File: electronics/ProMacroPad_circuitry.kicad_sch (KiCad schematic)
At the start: 8 parts, among them J1 Conn_01x06, J2 Conn_01x07, P1 Conn_02x20_Odd_Even, U1 quad_level_shifter

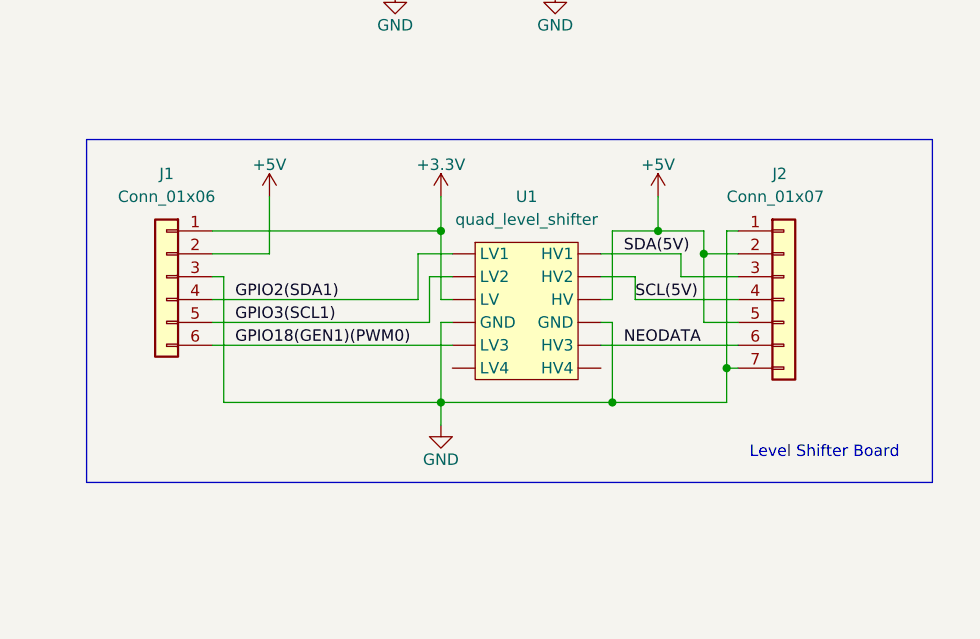
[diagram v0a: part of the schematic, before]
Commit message: Split apart connectors for LCD and keypad neopixel strip in the schematic
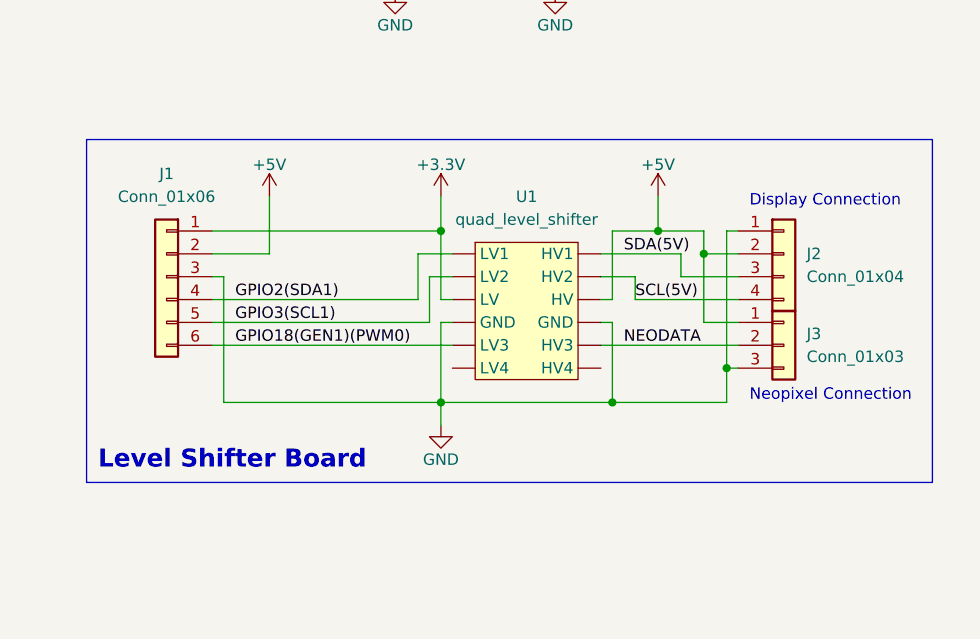
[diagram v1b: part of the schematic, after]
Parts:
- removed J2: Conn_01x07, Connector_PinHeader_2.54mm:PinHeader_1x05_P2.54mm_Vertical, symbol Connector_Generic:Conn_01x07
- added J2: Conn_01x04, Connector_PinHeader_2.54mm:PinHeader_1x04_P2.54mm_Vertical, symbol Connector_Generic:Conn_01x04
- added J3: Conn_01x03, Connector_PinHeader_2.54mm:PinHeader_1x03_P2.54mm_Vertical, symbol Connector_Generic:Conn_01x03
- P1: now left out of the parts list
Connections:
- net +5V: now also J2.2 (Pin_2), J3.1 (Pin_1)
- net GND: now also J2.1 (Pin_1), J3.3 (Pin_3)
- net NEODATA: now also J3.2 (Pin_2)
- net SCL(5V): now also J2.4 (Pin_4)
- net SDA(5V): now also J2.3 (Pin_3)
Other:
- note added: "Display Connection"
- note added: "Neopixel Connection"
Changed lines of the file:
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@@
     (effects (font (size 1.27 1.27)) (justify left bottom))
   )
-  (text "Level Shifter Board" (at 97.79 132.08 0)
+  (text "Display Connection\n" (at 97.79 104.14 0)
+    (effects (font (size 1.27 1.27)) (justify left bottom))
+  )
+  (text "Level Shifter Board" (at 25.4 133.35 0)
+    (effects (font (size 2 2) (thickness 0.254) bold) (justify left bottom))
+  )
+  (text "Neopixel Connection" (at 97.79 125.73 0)
     (effects (font (size 1.27 1.27)) (justify left bottom))
   )
@@
   (symbol (lib_id "power:+5V") (at 78.74 24.13 0) (unit 1)
     (in_bom yes) (on_board yes)
-    (property "Reference" "#PWR01" (id 0) (at 78.74 27.94 0)
+    (property "Reference" "#PWR07" (id 0) (at 78.74 27.94 0)
       (effects (font (size 1.27 1.27)) hide)
     )
@@
   (symbol (lib_id "power:+3.3V") (at 55.88 24.13 0) (unit 1)
     (in_bom yes) (on_board yes)
-    (property "Reference" "#PWR04" (id 0) (at 55.88 27.94 0)
+    (property "Reference" "#PWR02" (id 0) (at 55.88 27.94 0)
       (effects (font (size 1.27 1.27)) hide)
     )
@@
   (symbol (lib_id "power:GND") (at 76.2 80.01 0) (unit 1)
     (in_bom yes) (on_board yes)
-    (property "Reference" "#PWR02" (id 0) (at 76.2 86.36 0)
+    (property "Reference" "#PWR06" (id 0) (at 76.2 86.36 0)
       (effects (font (size 1.27 1.27)) hide)
     )
@@
   )
   (symbol (lib_id "Connector_Generic:Conn_02x20_Odd_Even") (at 66.04 50.8 0) (unit 1)
-    (in_bom yes) (on_board yes)
+    (in_bom no) (on_board no)
     (property "Reference" "P1" (id 0) (at 67.31 22.4282 0))
     (property "Value" "Conn_02x20_Odd_Even" (id 1) (at 67.31 24.7396 0))
@@
   (symbol (lib_id "power:+3.3V") (at 63.5 102.87 0) (unit 1)
     (in_bom yes) (on_board yes)
-    (property "Reference" "#PWR06" (id 0) (at 63.5 106.68 0)
+    (property "Reference" "#PWR04" (id 0) (at 63.5 106.68 0)
       (effects (font (size 1.27 1.27)) hide)
     )
@@
     (property "Datasheet" "" (id 3) (at 63.5 102.87 0))
     (pin "1")
+  )
+  (symbol (lib_id "Connector_Generic:Conn_01x03") (at 101.6 119.38 0) (unit 1)
+    (in_bom yes) (on_board yes) (fields_autoplaced)
+    (property "Reference" "J3" (id 0) (at 104.14 118.1099 0)
+      (effects (font (size 1.27 1.27)) (justify left))
+    )
+    (property "Value" "Conn_01x03" (id 1) (at 104.14 120.6499 0)
+      (effects (font (size 1.27 1.27)) (justify left))
+    )
+    (property "Footprint" "Connector_PinHeader_2.54mm:PinHeader_1x03_P2.54mm_Vertical" (id 2) (at 101.6 119.38 0)
+      (effects (font (size 1.27 1.27)) hide)
+    )
+    (property "Datasheet" "~" (id 3) (at 101.6 119.38 0)
+      (effects (font (size 1.27 1.27)) hide)
+    )
+    (pin "1")
+    (pin "2")
+    (pin "3")
   )
   (symbol (lib_id "Connector_Generic:Conn_01x06") (at 33.02 111.76 0) (mirror y) (unit 1)
@@
     (pin "6")
   )
-  (symbol (lib_id "Connector_Generic:Conn_01x07") (at 101.6 114.3 0) (unit 1)
-    (in_bom yes) (on_board yes)
-    (property "Reference" "J2" (id 0) (at 100.33 100.33 0)
-      (effects (font (size 1.27 1.27)) (justify left))
-    )
-    (property "Value" "Conn_01x07" (id 1) (at 95.25 102.87 0)
-      (effects (font (size 1.27 1.27)) (justify left))
-    )
-    (property "Footprint" "Connector_PinHeader_2.54mm:PinHeader_1x05_P2.54mm_Vertical" (id 2) (at 101.6 114.3 0)
-      (effects (font (size 1.27 1.27)) hide)
-    )
-    (property "Datasheet" "~" (id 3) (at 101.6 114.3 0)
-      (effects (font (size 1.27 1.27)) hide)
-    )
-    (pin "1")
-    (pin "2")
-    (pin "3")
-    (pin "4")
-    (pin "5")
-    (pin "6")
-    (pin "7")
-  )
   (symbol (lib_id "power:+5V") (at 44.45 102.87 0) (unit 1)
     (in_bom yes) (on_board yes)
-    (property "Reference" "#PWR05" (id 0) (at 44.45 106.68 0)
+    (property "Reference" "#PWR01" (id 0) (at 44.45 106.68 0)
       (effects (font (size 1.27 1.27)) hide)
     )
@@
   (symbol (lib_id "power:GND") (at 63.5 128.27 0) (unit 1)
     (in_bom yes) (on_board yes)
-    (property "Reference" "#PWR07" (id 0) (at 63.5 134.62 0)
+    (property "Reference" "#PWR05" (id 0) (at 63.5 134.62 0)
       (effects (font (size 1.27 1.27)) hide)
     )
@@
     (pin "")
   )
+  (symbol (lib_id "Connector_Generic:Conn_01x04") (at 101.6 109.22 0) (unit 1)
+    (in_bom yes) (on_board yes) (fields_autoplaced)
+    (property "Reference" "J2" (id 0) (at 104.14 109.2199 0)
+      (effects (font (size 1.27 1.27)) (justify left))
+    )
+    (property "Value" "Conn_01x04" (id 1) (at 104.14 111.7599 0)
+      (effects (font (size 1.27 1.27)) (justify left))
+    )
+    (property "Footprint" "Connector_PinHeader_2.54mm:PinHeader_1x04_P2.54mm_Vertical" (id 2) (at 101.6 109.22 0)
+      (effects (font (size 1.27 1.27)) hide)
+    )
+    (property "Datasheet" "~" (id 3) (at 101.6 109.22 0)
+      (effects (font (size 1.27 1.27)) hide)
+    )
+    (pin "1")
+    (pin "2")
+    (pin "3")
+    (pin "4")
+  )
   (sheet_instances
     (path "/" (page "1"))
   )
   (symbol_instances
-    (path "/00000000-0000-0000-0000-0000580c1b61"
+    (path "/9eacbb2d-50b8-4118-adfc-424ecd01793d"
       (reference "#PWR01") (unit 1) (value "+5V") (footprint "")
     )
-    (path "/00000000-0000-0000-0000-0000580c1d11"
-      (reference "#PWR02") (unit 1) (value "GND") (footprint "")
+    (path "/00000000-0000-0000-0000-0000580c1bc1"
+      (reference "#PWR02") (unit 1) (value "+3.3V") (footprint "")
     )
     (path "/00000000-0000-0000-0000-0000580c1e01"
       (reference "#PWR03") (unit 1) (value "GND") (footprint "")
     )
-    (path "/00000000-0000-0000-0000-0000580c1bc1"
+    (path "/2e9e347b-3a58-4bc6-a17d-c08a993af17a"
       (reference "#PWR04") (unit 1) (value "+3.3V") (footprint "")
     )
-    (path "/9eacbb2d-50b8-4118-adfc-424ecd01793d"
-      (reference "#PWR05") (unit 1) (value "+5V") (footprint "")
-    )
-    (path "/2e9e347b-3a58-4bc6-a17d-c08a993af17a"
-      (reference "#PWR06") (unit 1) (value "+3.3V") (footprint "")
-    )
     (path "/e8685b3e-eccd-4437-baaf-b2ee6240a83c"
-      (reference "#PWR07") (unit 1) (value "GND") (footprint "")
+      (reference "#PWR05") (unit 1) (value "GND") (footprint "")
+    )
+    (path "/00000000-0000-0000-0000-0000580c1d11"
+      (reference "#PWR06") (unit 1) (value "GND") (footprint "")
+    )
+    (path "/00000000-0000-0000-0000-0000580c1b61"
+      (reference "#PWR07") (unit 1) (value "+5V") (footprint "")
     )
     (path "/c6c3c7e1-1d0c-40e9-a9b5-621b98f4c1e6"
@@
       (reference "J1") (unit 1) (value "Conn_01x06") (footprint "Connector_PinHeader_2.54mm:PinHeader_1x06_P2.54mm_Vertical")
     )
-    (path "/986b7e4d-ecdc-467f-b1ac-492727860f1f"
-      (reference "J2") (unit 1) (value "Conn_01x07") (footprint "Connector_PinHeader_2.54mm:PinHeader_1x05_P2.54mm_Vertical")
+    (path "/f91c8543-b6dd-4522-a7f9-22fa2740e79b"
+      (reference "J2") (unit 1) (value "Conn_01x04") (footprint "Connector_PinHeader_2.54mm:PinHeader_1x04_P2.54mm_Vertical")
+    )
+    (path "/68d756a1-f19e-4dc7-a5af-e5afa6b979ac"
+      (reference "J3") (unit 1) (value "Conn_01x03") (footprint "Connector_PinHeader_2.54mm:PinHeader_1x03_P2.54mm_Vertical")
     )
     (path "/00000000-0000-0000-0000-00005834fb2e"

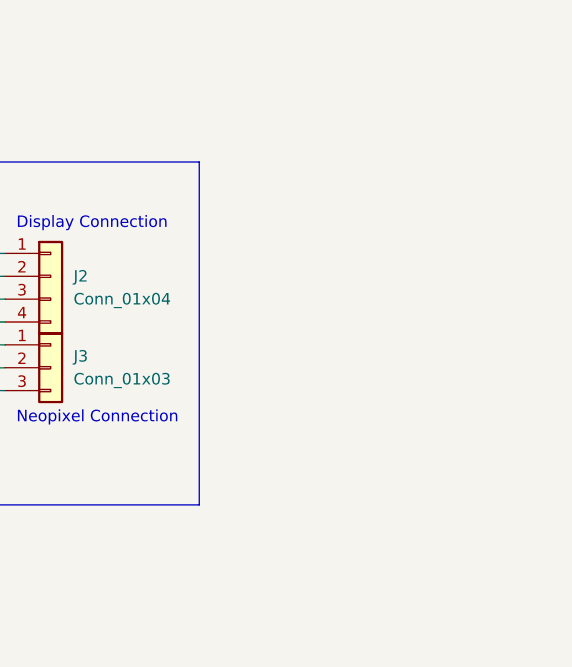
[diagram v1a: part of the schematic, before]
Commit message: added keypad matrix connectors to schematic
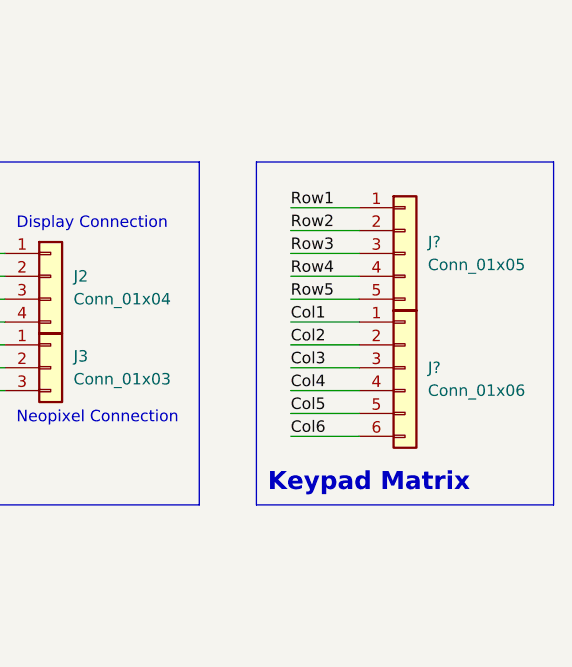
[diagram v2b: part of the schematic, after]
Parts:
- added J?: Conn_01x06, symbol Connector_Generic:Conn_01x06
- added J?: Conn_01x05, symbol Connector_Generic:Conn_01x05
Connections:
- new net Col1: J?.1 (Pin_1)
- new net Col2: J?.2 (Pin_2)
- new net Col3: J?.3 (Pin_3)
- new net Col4: J?.4 (Pin_4)
- new net Col5: J?.5 (Pin_5)
- new net Col6: J?.6 (Pin_6)
- new net Row1: J?.1 (Pin_1)
- new net Row2: J?.2 (Pin_2)
- new net Row3: J?.3 (Pin_3)
- new net Row4: J?.4 (Pin_4)
- new net Row5: J?.5 (Pin_5)
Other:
- note added: "Keypad Matrix"
- title: (none) -> ProMacroPad
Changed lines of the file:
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@@
   (paper "A4")
   (title_block
-    (date "15 nov 2012")
+    (title "ProMacroPad")
+    (date "2022-01-20")
   )
   (junction (at 82.55 125.73) (diameter 0) (color 0 0 0 0)
@@
   (junction (at 63.5 125.73) (diameter 0) (color 0 0 0 0)
   )
+  (wire (pts (xy 128.27 114.3) (xy 135.89 114.3))
+    (stroke (width 0) (type default) (color 0 0 0 0))
+  )
   (wire (pts (xy 92.71 109.22) (xy 92.71 116.84))
     (stroke (width 0) (type default) (color 0 0 0 0))
@@
     (stroke (width 0) (type default) (color 0 0 0 0))
   )
+  (wire (pts (xy 128.27 101.6) (xy 135.89 101.6))
+    (stroke (width 0) (type default) (color 0 0 0 0))
+  )
+  (wire (pts (xy 128.27 111.76) (xy 135.89 111.76))
+    (stroke (width 0) (type default) (color 0 0 0 0))
+  )
+  (polyline (pts (xy 124.46 96.52) (xy 157.48 96.52))
+    (stroke (width 0) (type default) (color 0 0 0 0))
+  )
   (wire (pts (xy 81.28 116.84) (xy 82.55 116.84))
     (stroke (width 0) (type default) (color 0 0 0 0))
@@
     (stroke (width 0) (type solid) (color 0 0 0 0))
   )
+  (wire (pts (xy 128.27 124.46) (xy 135.89 124.46))
+    (stroke (width 0) (type default) (color 0 0 0 0))
+  )
   (wire (pts (xy 60.96 60.96) (xy 31.75 60.96))
     (stroke (width 0) (type solid) (color 0 0 0 0))
@@
     (stroke (width 0) (type solid) (color 0 0 0 0))
   )
+  (wire (pts (xy 128.27 106.68) (xy 135.89 106.68))
+    (stroke (width 0) (type default) (color 0 0 0 0))
+  )
   (wire (pts (xy 60.96 30.48) (xy 31.75 30.48))
     (stroke (width 0) (type solid) (color 0 0 0 0))
@@
     (stroke (width 0) (type solid) (color 0 0 0 0))
   )
+  (wire (pts (xy 128.27 109.22) (xy 135.89 109.22))
+    (stroke (width 0) (type default) (color 0 0 0 0))
+  )
   (wire (pts (xy 95.25 121.92) (xy 95.25 125.73))
     (stroke (width 0) (type default) (color 0 0 0 0))
@@
     (stroke (width 0) (type default) (color 0 0 0 0))
   )
+  (wire (pts (xy 128.27 119.38) (xy 135.89 119.38))
+    (stroke (width 0) (type default) (color 0 0 0 0))
+  )
   (wire (pts (xy 38.1 109.22) (xy 44.45 109.22))
     (stroke (width 0) (type default) (color 0 0 0 0))
   )
+  (wire (pts (xy 128.27 104.14) (xy 135.89 104.14))
+    (stroke (width 0) (type default) (color 0 0 0 0))
+  )
   (wire (pts (xy 73.66 48.26) (xy 100.33 48.26))
     (stroke (width 0) (type solid) (color 0 0 0 0))
@@
     (stroke (width 0) (type solid) (color 0 0 0 0))
   )
+  (wire (pts (xy 128.27 127) (xy 135.89 127))
+    (stroke (width 0) (type default) (color 0 0 0 0))
+  )
   (polyline (pts (xy 24.13 96.52) (xy 118.11 96.52))
     (stroke (width 0) (type default) (color 0 0 0 0))
@@
     (stroke (width 0) (type default) (color 0 0 0 0))
   )
+  (wire (pts (xy 128.27 116.84) (xy 135.89 116.84))
+    (stroke (width 0) (type default) (color 0 0 0 0))
+  )
   (wire (pts (xy 31.75 43.18) (xy 60.96 43.18))
     (stroke (width 0) (type solid) (color 0 0 0 0))
@@
     (stroke (width 0) (type default) (color 0 0 0 0))
   )
+  (polyline (pts (xy 157.48 134.62) (xy 157.48 96.52))
+    (stroke (width 0) (type default) (color 0 0 0 0))
+  )
   (wire (pts (xy 73.66 55.88) (xy 100.33 55.88))
     (stroke (width 0) (type solid) (color 0 0 0 0))
@@
     (stroke (width 0) (type default) (color 0 0 0 0))
   )
+  (wire (pts (xy 128.27 121.92) (xy 135.89 121.92))
+    (stroke (width 0) (type default) (color 0 0 0 0))
+  )
+  (polyline (pts (xy 124.46 134.62) (xy 157.48 134.62))
+    (stroke (width 0) (type default) (color 0 0 0 0))
+  )
   (wire (pts (xy 95.25 121.92) (xy 96.52 121.92))
+    (stroke (width 0) (type default) (color 0 0 0 0))
+  )
+  (polyline (pts (xy 124.46 96.52) (xy 124.46 134.62))
     (stroke (width 0) (type default) (color 0 0 0 0))
   )
@@
     (effects (font (size 1.27 1.27)) (justify left bottom))
   )
+  (text "Keypad Matrix" (at 125.73 133.35 0)
+    (effects (font (size 2 2) (thickness 0.4) bold) (justify left bottom))
+  )
   (text "Level Shifter Board" (at 25.4 133.35 0)
     (effects (font (size 2 2) (thickness 0.254) bold) (justify left bottom))
@@
     (effects (font (size 1.27 1.27)) (justify right bottom))
   )
+  (label "Row1" (at 128.27 101.6 0)
+    (effects (font (size 1.27 1.27)) (justify left bottom))
+  )
   (label "GPIO25(GEN6)" (at 100.33 53.34 180)
     (effects (font (size 1.27 1.27)) (justify right bottom))
@@
     (effects (font (size 1.27 1.27)) (justify right bottom))
   )
+  (label "Col5" (at 128.27 124.46 0)
+    (effects (font (size 1.27 1.27)) (justify left bottom))
+  )
+  (label "Row2" (at 128.27 104.14 0)
+    (effects (font (size 1.27 1.27)) (justify left bottom))
+  )
   (label "NEODATA" (at 83.82 119.38 0)
     (effects (font (size 1.27 1.27)) (justify left bottom))
@@
     (effects (font (size 1.27 1.27)) (justify left bottom))
   )
+  (label "Col1" (at 128.27 114.3 0)
+    (effects (font (size 1.27 1.27)) (justify left bottom))
+  )
   (label "SCL(5V)" (at 85.09 114.3 0)
     (effects (font (size 1.27 1.27)) (justify left bottom))
@@
     (effects (font (size 1.27 1.27)) (justify left bottom))
   )
+  (label "Row3" (at 128.27 106.68 0)
+    (effects (font (size 1.27 1.27)) (justify left bottom))
+  )
   (label "GPIO16" (at 100.33 71.12 180)
     (effects (font (size 1.27 1.27)) (justify right bottom))
@@
     (effects (font (size 1.27 1.27)) (justify left bottom))
   )
+  (label "Row5" (at 128.27 111.76 0)
+    (effects (font (size 1.27 1.27)) (justify left bottom))
+  )
+  (label "Col3" (at 128.27 119.38 0)
+    (effects (font (size 1.27 1.27)) (justify left bottom))
+  )
+  (label "Col2" (at 128.27 116.84 0)
+    (effects (font (size 1.27 1.27)) (justify left bottom))
+  )
   (label "GPIO27(GEN2)" (at 31.75 43.18 0)
     (effects (font (size 1.27 1.27)) (justify left bottom))
@@
   )
   (label "SDA(5V)" (at 83.82 109.22 0)
+    (effects (font (size 1.27 1.27)) (justify left bottom))
+  )
+  (label "Col6" (at 128.27 127 0)
+    (effects (font (size 1.27 1.27)) (justify left bottom))
+  )
+  (label "Row4" (at 128.27 109.22 0)
+    (effects (font (size 1.27 1.27)) (justify left bottom))
+  )
+  (label "Col4" (at 128.27 121.92 0)
     (effects (font (size 1.27 1.27)) (justify left bottom))
   )
@@
     (pin "1")
   )
+  (symbol (lib_id "Connector_Generic:Conn_01x06") (at 140.97 119.38 0) (unit 1)
+    (in_bom yes) (on_board yes) (fields_autoplaced)
+    (property "Reference" "J?" (id 0) (at 143.51 119.3799 0)
+      (effects (font (size 1.27 1.27)) (justify left))
+    )
+    (property "Value" "Conn_01x06" (id 1) (at 143.51 121.9199 0)
+      (effects (font (size 1.27 1.27)) (justify left))
+    )
+    (property "Footprint" "" (id 2) (at 140.97 119.38 0)
+      (effects (font (size 1.27 1.27)) hide)
+    )
+    (property "Datasheet" "~" (id 3) (at 140.97 119.38 0)
+      (effects (font (size 1.27 1.27)) hide)
+    )
+    (pin "1")
+    (pin "2")
+    (pin "3")
+    (pin "4")
+    (pin "5")
+    (pin "6")
+  )
   (symbol (lib_id "Connector_Generic:Conn_01x03") (at 101.6 119.38 0) (unit 1)
     (in_bom yes) (on_board yes) (fields_autoplaced)
@@
     (pin "2")
     (pin "3")
+  )
+  (symbol (lib_id "Connector_Generic:Conn_01x05") (at 140.97 106.68 0) (unit 1)
+    (in_bom yes) (on_board yes) (fields_autoplaced)
+    (property "Reference" "J?" (id 0) (at 143.51 105.4099 0)
+      (effects (font (size 1.27 1.27)) (justify left))
+    )
+    (property "Value" "Conn_01x05" (id 1) (at 143.51 107.9499 0)
+      (effects (font (size 1.27 1.27)) (justify left))
+    )
+    (property "Footprint" "" (id 2) (at 140.97 106.68 0)
+      (effects (font (size 1.27 1.27)) hide)
+    )
+    (property "Datasheet" "~" (id 3) (at 140.97 106.68 0)
+      (effects (font (size 1.27 1.27)) hide)
+    )
+    (pin "1")
+    (pin "2")
+    (pin "3")
+    (pin "4")
+    (pin "5")
   )
   (symbol (lib_id "Connector_Generic:Conn_01x06") (at 33.02 111.76 0) (mirror y) (unit 1)
@@
       (reference "J3") (unit 1) (value "Conn_01x03") (footprint "Connector_PinHeader_2.54mm:PinHeader_1x03_P2.54mm_Vertical")
     )
+    (path "/5dcf572f-bb8e-45c7-87f9-4b8e5d71a2b0"
+      (reference "J?") (unit 1) (value "Conn_01x06") (footprint "")
+    )
+    (path "/6f40dec4-e7fa-4828-8490-031dc1244e04"
+      (reference "J?") (unit 1) (value "Conn_01x05") (footprint "")
+    )
     (path "/00000000-0000-0000-0000-00005834fb2e"
